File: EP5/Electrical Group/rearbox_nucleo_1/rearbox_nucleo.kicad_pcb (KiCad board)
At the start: 2 copper layers, 106 x 73.2 mm, 47 parts, among them IC1 CTM1051AM, J1 STM5V, J10 CAN_Rpi, J11 fan1, J12 fan2, J13 buzzer, J14 CAN, J15 APPS_BSE, J2 steering, J4 5V, J5 VCC_3V3, J6 sensor_R, J7 sensor_L, J8 24V, J9 Rpi, P1 24Vpower, Q1 PN2222A, U1 NUCLEOH723ZG_WITHOUT_MORHPHO, U2 LMV358, U4 TEN_40-2411WIE

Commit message: update rear box nucleo
but only connector symbols
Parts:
- removed C1: 10u, Capacitor_SMD:C_0805_2012Metric_Pad1.18x1.45mm_HandSolder
- removed C2: 0u1, Capacitor_SMD:C_0603_1608Metric
- removed C3: 1n, Capacitor_THT:C_Disc_D5.0mm_W2.5mm_P5.00mm
- removed C4: 0u1, Capacitor_Tantalum_SMD:CP_EIA-3528-21_Kemet-B_Pad1.50x2.35mm_HandSolder
- removed D1: LED4, LED_SMD:LED_0603_1608Metric_Pad1.05x0.95mm_HandSolder
- removed F1: Polyfuse_Small, Fuse:Fuse_1206_3216Metric
- removed H1, H2, H3, H4: MountingHole_Pad, MountingHole:MountingHole_2.2mm_M2_DIN965_Pad
- removed IC1: CTM1051AM, SamacSys_Parts:CTM1051AM
- removed J1: STM5V, Connector_PinHeader_2.54mm:PinHeader_1x02_P2.54mm_Vertical
- removed J10: CAN_Rpi, Connector_JST:JST_XH_S3B-XH-A-1_1x03_P2.50mm_Horizontal
- removed J11: fan1, Connector_PinHeader_2.54mm:PinHeader_1x03_P2.54mm_Vertical
- removed J12: fan2, Connector_PinHeader_2.54mm:PinHeader_1x03_P2.54mm_Vertical
- removed J13: buzzer, Connector_JST:JST_XH_B2B-XH-A_1x02_P2.50mm_Vertical
- removed J14: CAN, Connector_JST:JST_XH_S3B-XH-A-1_1x03_P2.50mm_Horizontal
- removed J15: APPS_BSE, Connector_JST:JST_XH_B10B-XH-A_1x10_P2.50mm_Vertical
- removed J2: steering, Connector_JST:JST_XH_B6B-XH-A_1x06_P2.50mm_Vertical
- removed J4: 5V, Connector_PinSocket_2.54mm:PinSocket_1x02_P2.54mm_Vertical
- removed J5: VCC_3V3, Connector_PinSocket_2.54mm:PinSocket_1x02_P2.54mm_Vertical
- removed J6: sensor_R, Connector_JST:JST_XH_B7B-XH-A_1x07_P2.50mm_Vertical
- removed J7: sensor_L, Connector_JST:JST_XH_S9B-XH-A-1_1x09_P2.50mm_Horizontal
- removed J8: 24V, Connector_PinSocket_2.54mm:PinSocket_1x02_P2.54mm_Vertical
- removed J9: Rpi, Connector_JST:JST_XH_S5B-XH-A-1_1x05_P2.50mm_Horizontal
- removed P1: 24Vpower, Connector_JST:JST_XH_B2B-XH-A_1x02_P2.50mm_Vertical
- removed Q1: PN2222A, Package_TO_SOT_THT:TO-92_Inline
- removed R1, R2: 10k, Resistor_SMD:R_0603_1608Metric
- removed R10: 2k7, Resistor_SMD:R_0603_1608Metric
- removed R11: 3k6, Resistor_SMD:R_0603_1608Metric
- removed R12, R13, R8, R9: 4k7, Resistor_SMD:R_0603_1608Metric
- removed R14, R15, R17: 1k, Resistor_SMD:R_0603_1608Metric
- removed R16: 100, Resistor_SMD:R_0603_1608Metric
- removed R3: 120, Resistor_SMD:R_1206_3216Metric
- removed R4: 1M, Resistor_SMD:R_0603_1608Metric
- removed R5, R6, R7: 100k, Resistor_SMD:R_0603_1608Metric
- removed U1: NUCLEOH723ZG_WITHOUT_MORHPHO, nturt_kicad_lib:MODULE_NUCLEOH723ZG_WITHOUT_MORHPHO
- removed U2: LMV358, Package_SO:SOIC-8_3.9x4.9mm_P1.27mm
- removed U4: TEN_40-2411WIE, SamacSys_Parts:TEN402411WIE
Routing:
- net VCC: track 331.0 -> 0.00 mm, vias 2 -> 0
- net +5V: track 301.4 -> 0.00 mm, vias 2 -> 0
- net MOSI: track 106.4 -> 0.00 mm
- net MISO: track 95.6 -> 0.00 mm
- net travel_L: track 94.5 -> 0.00 mm
- net SS: track 79.6 -> 0.00 mm
- net SCK: track 70.2 -> 0.00 mm
- net hall_L: track 64.9 -> 0.00 mm
- net Net-(J9-Pin_5): track 41.3 -> 0.00 mm
- net 24V: track 40.8 -> 0.00 mm
- net oilPressure: track 37.5 -> 0.00 mm
- net CANH: track 37.3 -> 0.00 mm
- net SDA_L: track 34.8 -> 0.00 mm
- net SCL_L: track 33.1 -> 0.00 mm
- net SCL_R: track 32.6 -> 0.00 mm
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- removed copper zone on F.Cu, net +5V
- removed copper zone on B.Cu, net CANG
- removed copper zone on B.Cu, net GND
- removed copper zone on F.Cu, net GND
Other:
- board outline removed

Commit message: 1st layout for rearbox nucleo done
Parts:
- added C1: 100n, Capacitor_SMD:C_0805_2012Metric, F.Cu at (141.7, 102.3)
- added C10: 1u, Capacitor_SMD:C_0805_2012Metric, F.Cu at (163.1, 63.7)
- added C11: 1u, Capacitor_SMD:C_0805_2012Metric, F.Cu at (149.1, 63.7)
- added C12: 1u, Capacitor_SMD:C_0805_2012Metric, F.Cu at (159.0, 63.7)
- added C13: 1u, Capacitor_SMD:C_0805_2012Metric, F.Cu at (145.5, 63.7)
- added C14: 100n, Capacitor_SMD:C_0805_2012Metric, F.Cu at (132.3, 134.8)
- added C15: 100n, Capacitor_SMD:C_0805_2012Metric, F.Cu at (129.4, 114.6)
- added C16: 330p, Capacitor_SMD:C_0805_2012Metric, F.Cu at (132.8, 129.0)
- added C17: 330p, Capacitor_SMD:C_0805_2012Metric, F.Cu at (133.5, 107.4)
- added C18: 1n, Capacitor_SMD:C_0805_2012Metric, F.Cu at (127.5, 119.6)
- added C19: 1n, Capacitor_SMD:C_0805_2012Metric, F.Cu at (130.3, 98.0)
- added C2: 100u, Capacitor_THT:C_Radial_D6.3mm_H11.0mm_P2.50mm, F.Cu at (125.2, 71.9)
- added C20: 1n, Capacitor_SMD:C_0805_2012Metric, F.Cu at (124.3, 122.4)
- added C21: 1n, Capacitor_SMD:C_0805_2012Metric, F.Cu at (126.0, 101.6)
- added C22: 100n, Capacitor_SMD:C_0805_2012Metric, F.Cu at (127.8, 122.4)
- added C23: 100n, Capacitor_SMD:C_0805_2012Metric, F.Cu at (130.0, 101.6)
- added C24: 100n, Capacitor_SMD:C_0805_2012Metric, F.Cu at (121.1, 135.6)
- added C25: 100n, Capacitor_SMD:C_0805_2012Metric, F.Cu at (122.3, 114.6)
- added C3: 100n, Capacitor_SMD:C_0805_2012Metric, F.Cu at (141.7, 108.4)
- added C4: 220p, Capacitor_SMD:C_0805_2012Metric, F.Cu at (167.6, 119.9)
- added C5: 220p, Capacitor_SMD:C_0805_2012Metric, F.Cu at (159.5, 133.1)
- added C6: 220p, Capacitor_SMD:C_0805_2012Metric, F.Cu at (163.0, 112.5)
- added C7: 220p, Capacitor_SMD:C_0805_2012Metric, F.Cu at (159.5, 125.5)
- added C8: 100n, Capacitor_SMD:C_0805_2012Metric, F.Cu at (169.4, 80.3)
- added C9: 100n, Capacitor_SMD:C_0805_2012Metric, F.Cu at (128.5, 92.7)
- added D1: 1N4148, Diode_SMD:D_0805_2012Metric, F.Cu at (112.5, 75.9)
- added D2: 1N4148, Diode_SMD:D_0805_2012Metric, F.Cu at (132.1, 73.9)
- added D3: 1N4148, Diode_SMD:D_0805_2012Metric, F.Cu at (163.7, 119.9)
- added D4: 1N4148, Diode_SMD:D_0805_2012Metric, F.Cu at (159.0, 112.5)
- added IC1: AP7375-50SA-7, SamacSys_Parts:SOT96P240X110-3N, F.Cu at (141.7, 105.4)
- added IC2: TLP5702_TP,E, SamacSys_Parts:SOT127P1000X230-6N, F.Cu at (127.5, 85.0)
- added IC3: ACS724LLCTR-05AB-T, SamacSys_Parts:SOIC127P600X175-8N, F.Cu at (133.4, 120.7)
- added IC4: ACS724LLCTR-05AB-T, SamacSys_Parts:SOIC127P600X175-8N, F.Cu at (135.5, 99.4)
- added IC5: AMC1200SDUBR, SamacSys_Parts:SOP254P1040X485-8N, F.Cu at (125.1, 129.0)
- added IC6: AMC1200SDUBR, SamacSys_Parts:SOP254P1040X485-8N, F.Cu at (125.9, 108.2)
- added J1: reset, Connector_JST:JST_XH_B2B-XH-A_1x02_P2.50mm_Vertical, F.Cu at (120.7, 94.0)
- added J10: front 24V, Connector_JST:JST_XH_B2B-XH-A_1x02_P2.50mm_Vertical, F.Cu at (168.1, 102.4)
- added J11: suspension RL, Connector_JST:JST_XH_B3B-XH-A_1x03_P2.50mm_Vertical, F.Cu at (158.6, 58.7)
- added J12: suspension RR, Connector_JST:JST_XH_B3B-XH-A_1x03_P2.50mm_Vertical, F.Cu at (144.6, 58.7)
- added J13: brake light, Connector_JST:JST_XH_B2B-XH-A_1x02_P2.50mm_Vertical, F.Cu at (149.6, 71.9)
- added J14: rear CAN, Connector_JST:JST_XH_B3B-XH-A_1x03_P2.50mm_Vertical, F.Cu at (175.5, 78.0)
- added J15: oilpressure, Connector_JST:JST_XH_B4B-XH-A_1x04_P2.50mm_Vertical, F.Cu at (140.7, 121.7)
- added J2: test_5V, Connector_PinHeader_2.54mm:PinHeader_1x02_P2.54mm_Vertical, F.Cu at (163.8, 66.8)
- added J3: test_3V3, Connector_PinHeader_2.54mm:PinHeader_1x02_P2.54mm_Vertical, F.Cu at (156.5, 66.8)
- added J4: test_5Vpwr, Connector_PinHeader_2.54mm:PinHeader_1x02_P2.54mm_Vertical, F.Cu at (147.3, 120.7)
- added J5: test_24V, Connector_PinHeader_2.54mm:PinHeader_1x02_P2.54mm_Vertical, F.Cu at (147.3, 114.1)
- added J6: power board, Connector_JST:JST_XH_B4B-XH-A_1x04_P2.50mm_Vertical, F.Cu at (157.5, 102.4)
- added J7: buzzer, Connector_JST:JST_XH_B2B-XH-A_1x02_P2.50mm_Vertical, F.Cu at (137.7, 71.9)
- added J8: pedal & steering, Connector_JST:JST_XH_B8B-XH-A_1x08_P2.50mm_Vertical, F.Cu at (152.9, 129.3)
- added J9: front CAN, Connector_JST:JST_XH_B3B-XH-A_1x03_P2.50mm_Vertical, F.Cu at (176.5, 59.2)
- added K1: Relay_SPST-NO, Relay_THT:Relay_SPST_Omron_G2RL-1A-E, F.Cu at (113.4, 66.2)
- added Q1: 2SC1945, Package_TO_SOT_THT:TO-220-3_Vertical, F.Cu at (118.6, 71.1)
- added R1: R_Small, Resistor_SMD:R_0805_2012Metric, F.Cu at (112.5, 82.3)
- added R10: 220R, Resistor_SMD:R_0805_2012Metric, F.Cu at (126.2, 92.7)
- added R11: 4R7, Resistor_THT:R_Axial_DIN0516_L15.5mm_D5.0mm_P5.08mm_Vertical, F.Cu at (138.9, 81.0)
- added R12: shunt, Resistor_SMD:R_0805_2012Metric, F.Cu at (135.4, 128.9)
- added R13: shunt, Resistor_SMD:R_0805_2012Metric, F.Cu at (136.1, 107.4)
- added R14: 12R, Resistor_SMD:R_0805_2012Metric, F.Cu at (134.6, 131.8)
- added R15: 12R, Resistor_SMD:R_0805_2012Metric, F.Cu at (134.6, 126.0)
- added R16: 12R, Resistor_SMD:R_0805_2012Metric, F.Cu at (135.0, 110.5)
- added R17: 12R, Resistor_SMD:R_0805_2012Metric, F.Cu at (135.0, 104.4)
- added R2: 4k7, Resistor_SMD:R_0805_2012Metric, F.Cu at (163.7, 117.3)
- added R3: 4k7, Resistor_SMD:R_0805_2012Metric, F.Cu at (166.9, 116.4)
- added R4: 60R, Resistor_SMD:R_0805_2012Metric, F.Cu at (162.5, 134.1)
- added R5: 60R, Resistor_SMD:R_0805_2012Metric, F.Cu at (162.5, 132.1)
- added R6: 4k7, Resistor_SMD:R_0805_2012Metric, F.Cu at (159.0, 110.0)
- added R7: 4k7, Resistor_SMD:R_0805_2012Metric, F.Cu at (163.0, 110.0)
- added R8: 60R, Resistor_SMD:R_0805_2012Metric, F.Cu at (162.5, 128.0)
- added R9: 60R, Resistor_SMD:R_0805_2012Metric, F.Cu at (162.5, 125.5)
- added RV1: 2R2, Potentiometer_THT:Potentiometer_Piher_T-16H_Single_Horizontal, F.Cu at (148.3, 93.2)
- added U1: NUCLEO-G474RE, nturt_kicad_lib:MODULE_NUCLEO-G474RE, F.Cu at (145.0, 96.4)
- added U3: MAX487E, Package_SO:SOIC-8_3.9x4.9mm_P1.27mm, F.Cu at (168.1, 133.6)
- added U4: MAX487E, Package_SO:SOIC-8_3.9x4.9mm_P1.27mm, F.Cu at (168.1, 127.0)
- added U5: LM317L_TO92, Package_TO_SOT_THT:TO-220-3_Vertical, F.Cu at (133.6, 84.1)
- added U6: TJA1051T-3, Package_SO:SOIC-8_3.9x4.9mm_P1.27mm, F.Cu at (169.4, 74.9)
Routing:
- net +5V: track 0.00 -> 383.0 mm, vias 0 -> 8
- net GNDPWR: track 0.00 -> 276.7 mm
- net +24V: track 0.00 -> 125.8 mm
- net +3V3: track 0.00 -> 117.0 mm, vias 0 -> 2
- net +5VD: track 0.00 -> 66.2 mm
- net suspension_RR: track 0.00 -> 58.2 mm
- net suspension_RL: track 0.00 -> 49.1 mm
- net GND: track 0.00 -> 45.6 mm, vias 0 -> 21
- net oilpressure_current_2: track 0.00 -> 43.9 mm
- net Net-(J13-Pin_2): track 0.00 -> 35.9 mm
- net CAN_RX: track 0.00 -> 30.5 mm
- net CAN_TX: track 0.00 -> 28.5 mm
- net RS485_2_RX: track 0.00 -> 28.1 mm
- net buzzer_switch: track 0.00 -> 27.2 mm
- net brake_trigger: track 0.00 -> 26.9 mm
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- added copper zone on F.Cu, net APPSmicro
- added copper zone on B.Cu, net GND
- added copper zone on F.Cu, net brakemicro
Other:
- board outline added: 71.6 x 83.1 mm

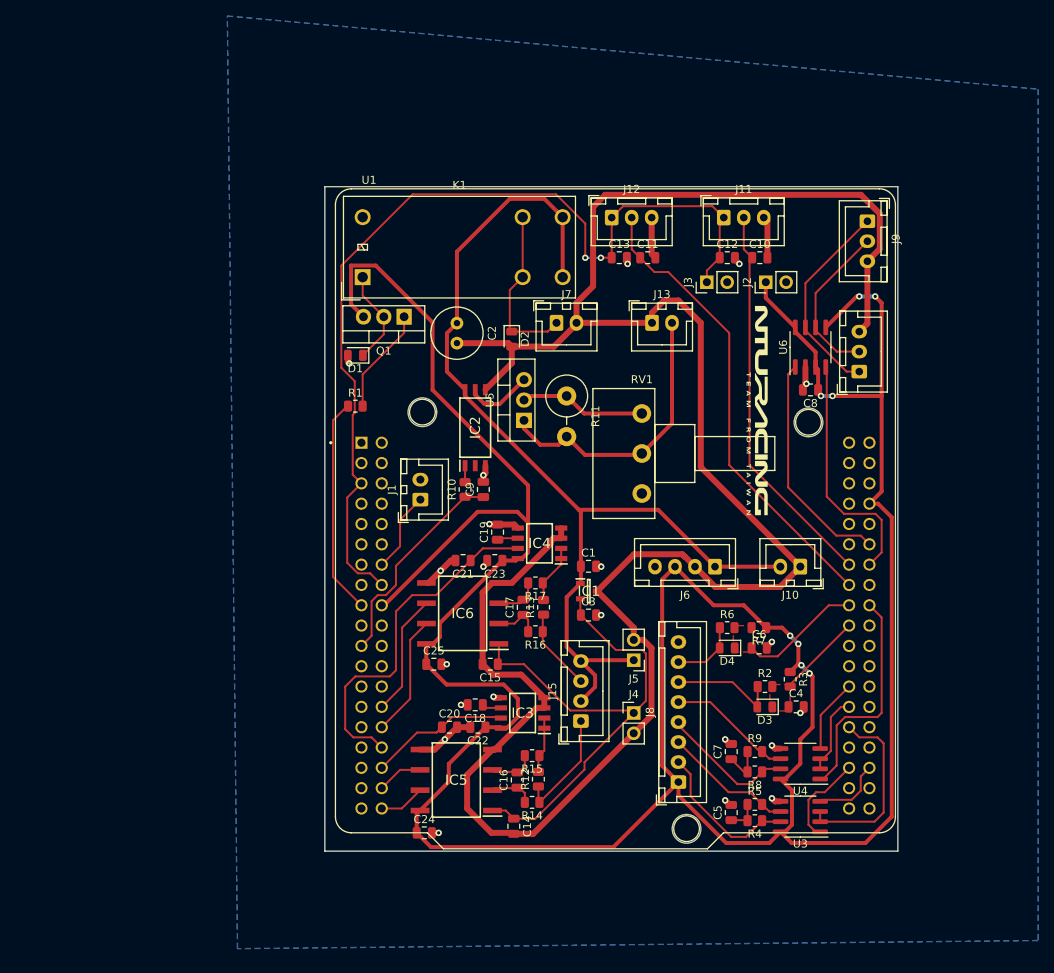
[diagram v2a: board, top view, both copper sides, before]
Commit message: update rearbox nucleo 1
mainly make a plane for GNDPWR
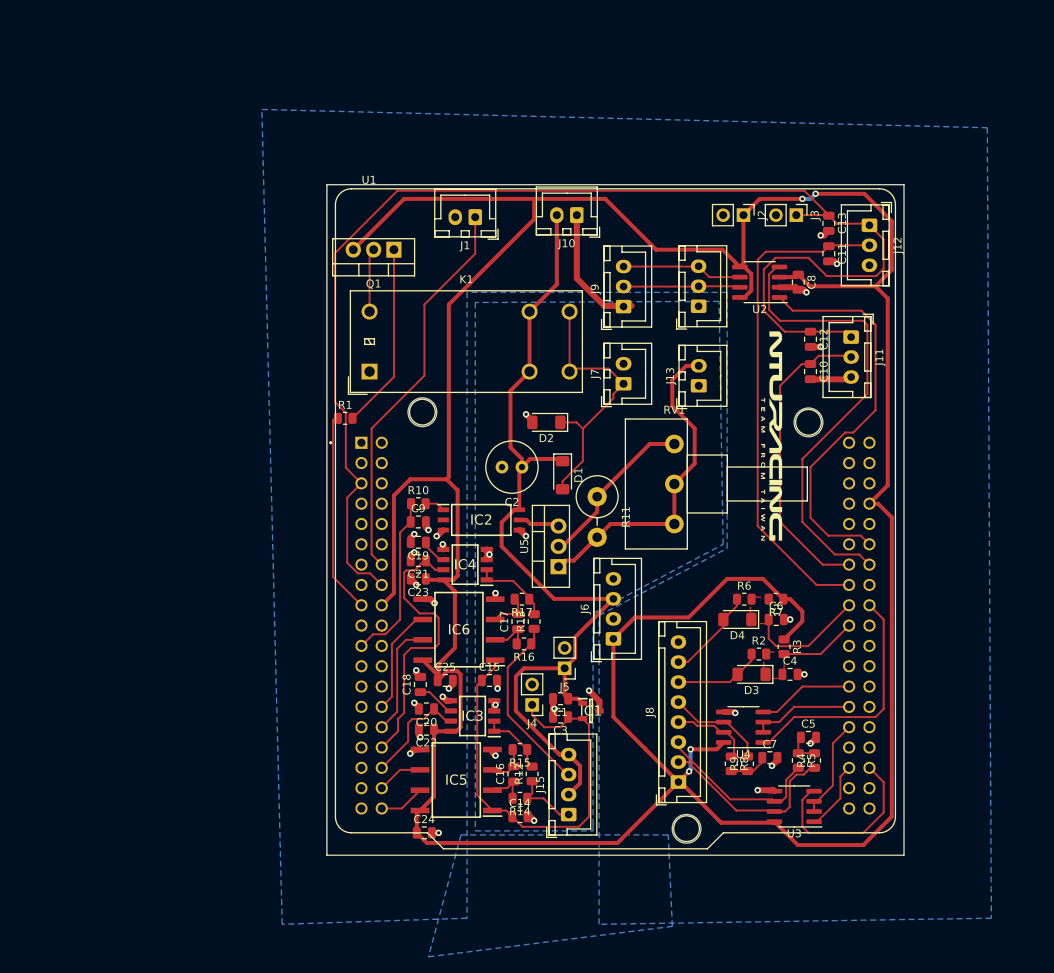
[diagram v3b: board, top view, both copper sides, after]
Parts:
- removed U6: TJA1051T-3, Package_SO:SOIC-8_3.9x4.9mm_P1.27mm
- added U2: TJA1051T-3, Package_SO:SOIC-8_3.9x4.9mm_P1.27mm, F.Cu at (163.1, 66.8)
- C1: value 100n -> 1u
- C3: value 100n -> 10u
- D1, D2, D3, D4: footprint Diode_SMD:D_0805_2012Metric -> Diode_SMD:D_MiniMELF
- moved J10 52.1 mm to (140.2, 58.4)
- moved J1 36.0 mm to (127.5, 58.7), turned to 180 degrees
- moved J9 32.3 mm to (146.1, 69.8), turned to 90 degrees
- moved J12 32.2 mm to (176.8, 59.7), turned to -90 degrees
- moved D1 29.9 mm to (138.4, 90.9), turned to -90 degrees
- moved C13 26.5 mm to (171.7, 59.4), turned to -90 degrees
- moved C11 22.6 mm to (171.7, 63.2), turned to -90 degrees
- moved J11 21.8 mm to (174.5, 73.7), turned to -90 degrees
- moved J14 21.7 mm to (155.4, 69.8)
- moved C2 19.7 mm to (133.3, 89.9), turned to 180 degrees
- moved U5 18.8 mm to (137.9, 102.4)
- moved C1 16.9 mm to (138.2, 118.9), turned to 180 degrees
- moved C10 15.6 mm to (169.4, 78.0), turned to -90 degrees
- moved J6 15.6 mm to (144.8, 111.4), turned to 90 degrees
- moved IC1 15.0 mm to (142.0, 120.4)
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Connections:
- C1 pad 2: GND -> GNDPWR
- C3 pad 2: GND -> GNDPWR
- D1 pad 1: Net-(D1-K) -> +24V
- D1 pad 2: GND -> Net-(D1-A)
- D2 pad 1: Net-(D2-K) -> Net-(D1-A)
- J14 pad 1: CANH -> GNDPWR
- J14 pad 2: CANL -> CANH
- J14 pad 3: GNDPWR -> CANL
- J6 pad 1: +24V -> +5V
- J6 pad 2: GNDPWR -> GND
- J6 pad 3: +5V -> +24V
- J6 pad 4: GND -> GNDPWR
- J7 pad 1: Net-(D2-K) -> Net-(D1-A)
- J9 pad 1: CANH -> GNDPWR
- J9 pad 2: CANL -> CANH
- J9 pad 3: GNDPWR -> CANL
- K1 pad 13: Net-(D2-K) -> +24V
- K1 pad 14: +24V -> Net-(D1-A)
- K1 pad A1: Net-(D1-K) -> GND
- K1 pad A2: GND -> Net-(Q1-E)
- Q1 pad 2: Net-(D1-K) -> Net-(Q1-E)
- RV1 pad 1: unconnected-(RV1-Pad1) -> Net-(J13-Pin_2)
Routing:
- net GNDPWR: track 276.7 -> 31.0 mm, vias 0 -> 10
- net +5V: track 383.0 -> 433.7 mm, vias 8 -> 4
- net +3V3: track 117.0 -> 162.7 mm, vias 2 -> 0
- net RESET: track 10.1 -> 49.3 mm
- net Net-(D1-A): track 0.00 -> 34.7 mm
- net CAN_RX: track 30.5 -> 57.8 mm
- net CAN_TX: track 28.5 -> 50.2 mm
- net Net-(D2-K): track 21.1 -> 0.00 mm
- net +24V: track 125.8 -> 111.2 mm
- net RS485_1_TX: track 8.94 -> 23.1 mm
- net brakePressure2: track 10.3 -> 22.8 mm
- net Net-(D1-K): track 12.0 -> 0.00 mm
- net CANH: track 25.7 -> 14.6 mm
- net RS485_1_mode: track 23.5 -> 12.6 mm
- net suspension_RL: track 49.1 -> 38.4 mm
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- added copper zone on B.Cu, net GNDPWR
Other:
- board size 71.6 x 83.1 mm -> 72.1 x 83.8 mm

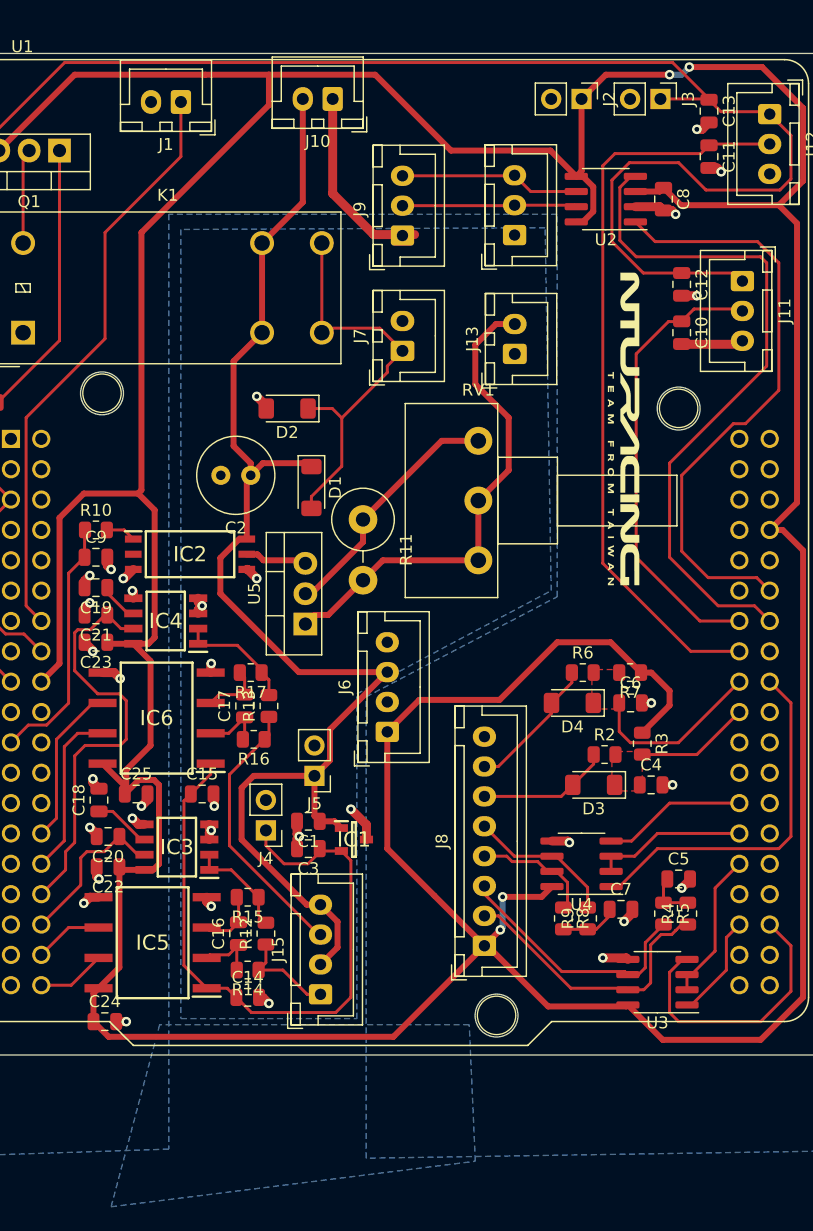
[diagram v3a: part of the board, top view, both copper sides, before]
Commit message: update rearbox nucleo 1 (mainly switch debounce)
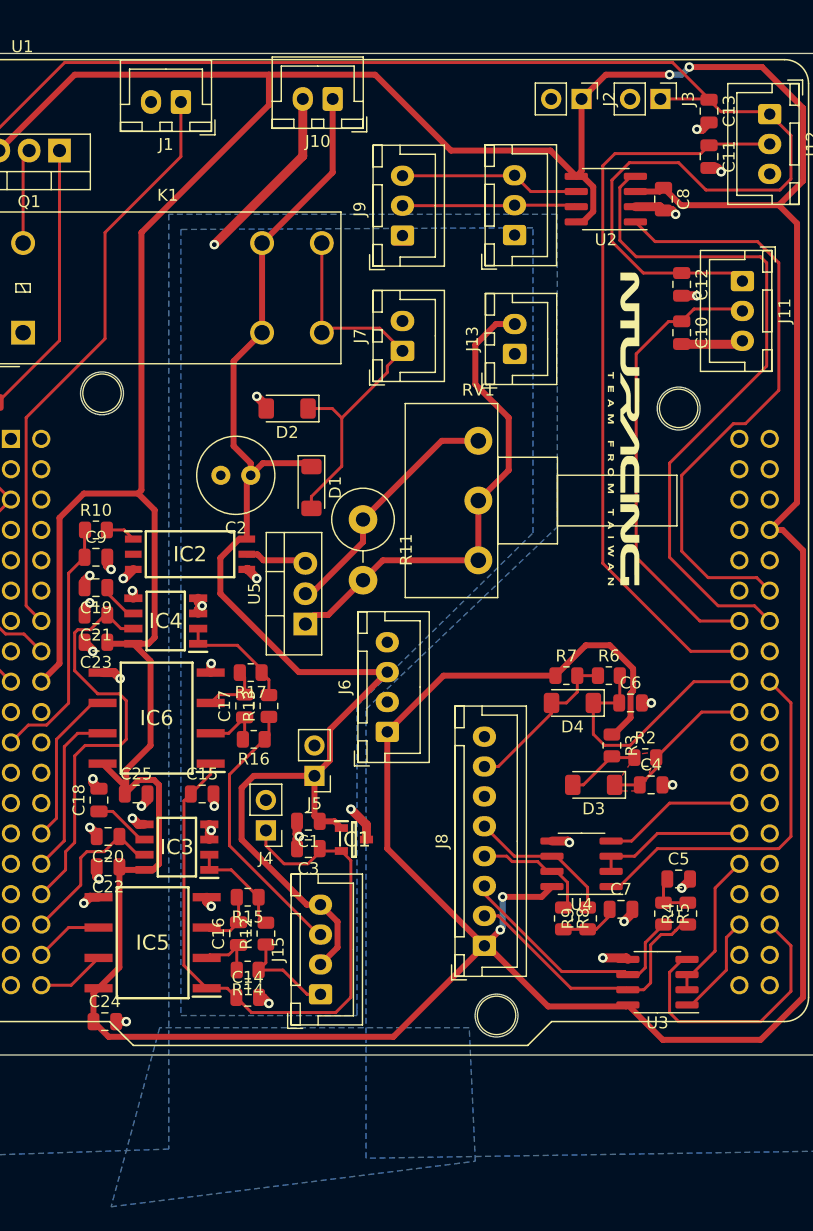
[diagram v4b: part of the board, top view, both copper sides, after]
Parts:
- moved R7 5.34 mm to (159.8, 106.7), turned to 0 degrees
- moved R2 3.41 mm to (166.4, 113.5)
- moved R3 2.54 mm to (163.6, 112.5)
- moved R6 2.20 mm to (163.3, 106.7)
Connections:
- J10 pad 1: GNDPWR -> +24V
- J10 pad 2: +24V -> GNDPWR
- R3 pad 2: APPSmicro -> APPSmicro_raw
- R7 pad 2: brakemicro -> brakemicro_raw
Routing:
- net brakemicro: track 15.0 -> 21.9 mm
- net APPSmicro_raw: track 11.1 -> 6.19 mm
- net APPSmicro: track 9.60 -> 13.5 mm
- net brakemicro_raw: track 11.6 -> 14.0 mm
- net +5V: track 433.7 -> 431.5 mm
- net +24V: track 111.2 -> 112.3 mm
- net GNDPWR: track 31.0 -> 30.0 mm, vias 10 -> 11
- removed copper zone on F.Cu, net brakemicro
